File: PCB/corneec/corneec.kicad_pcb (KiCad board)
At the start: 2 copper layers, 226.8 x 157.6 mm, 80 parts, among them J1 OLED, J2 MJ-4PP-9, Q1 Q_NMOS_GSD, SW1 SW_Push, SW10 EC_SW, SW11 EC_SW, SW12 EC_SW, SW13 EC_SW, SW14 EC_SW, SW15 EC_SW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

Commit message: Update
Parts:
- removed the ? at (156.3, 68.6)
- removed the ? at (156.3, 49.9)
- removed the ? at (241.8, 47.4)
- removed the ? at (248.7, 95.2)
- removed the ? at (256.1, 112.6)
- removed the ? at (199.5, 85.9)
- removed the SW2 at (241.8, 56.9)
- removed the SW2 at (146.8, 59.2)
- removed the SW2 at (146.8, 40.2)
- removed the SW2 at (165.8, 40.2)
- removed the SW2 at (241.8, 75.9)
- removed the SW2 at (222.8, 35.5)
- removed the SW2 at (203.8, 71.1)
- removed the SW2 at (241.8, 37.9)
- removed the SW2 at (203.8, 52.1)
- removed the SW2 at (256.5, 99.6)
- removed the SW2 at (165.8, 59.2)
- removed the SW2 at (184.8, 35.5)
- removed the SW2 at (146.8, 78.2)
- removed the SW2 at (222.8, 73.5)
- removed the SW2 at (184.8, 54.5)
- removed the SW2 at (234.3, 95.9)
- removed the SW2 at (165.8, 78.2)
- removed the SW2 at (222.8, 54.5)
- removed the SW2 at (213.3, 93.2)
- removed the SW2 at (203.8, 33.1)
- removed the SW2 at (184.8, 73.5)
- moved ? 55.4 mm to (188.8, 97.3)
- moved C2 55.4 mm to (199.9, 104.3)
- moved H22 55.4 mm to (203.3, 105.8)
- moved J1 55.4 mm to (195.9, 89.5)
- moved J2 55.4 mm to (205.7, 98.6)
- moved JP2 55.4 mm to (186.0, 52.0)
- moved R2 55.4 mm to (158.9, 63.5)
- moved R3 55.4 mm to (181.1, 65.8)
- moved R4 55.4 mm to (120.9, 63.5)
- moved R5 55.4 mm to (101.9, 68.2)
- moved R7 55.4 mm to (82.9, 68.2)
- moved REF** 55.4 mm to (176.0, 65.8)
- moved REF** 55.4 mm to (90.5, 87.1)
- moved REF** 55.4 mm to (90.5, 68.3)
- moved SW10 55.4 mm to (119.0, 92.0)
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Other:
- board size 226.8 x 157.6 mm -> 133.8 x 91.4 mm

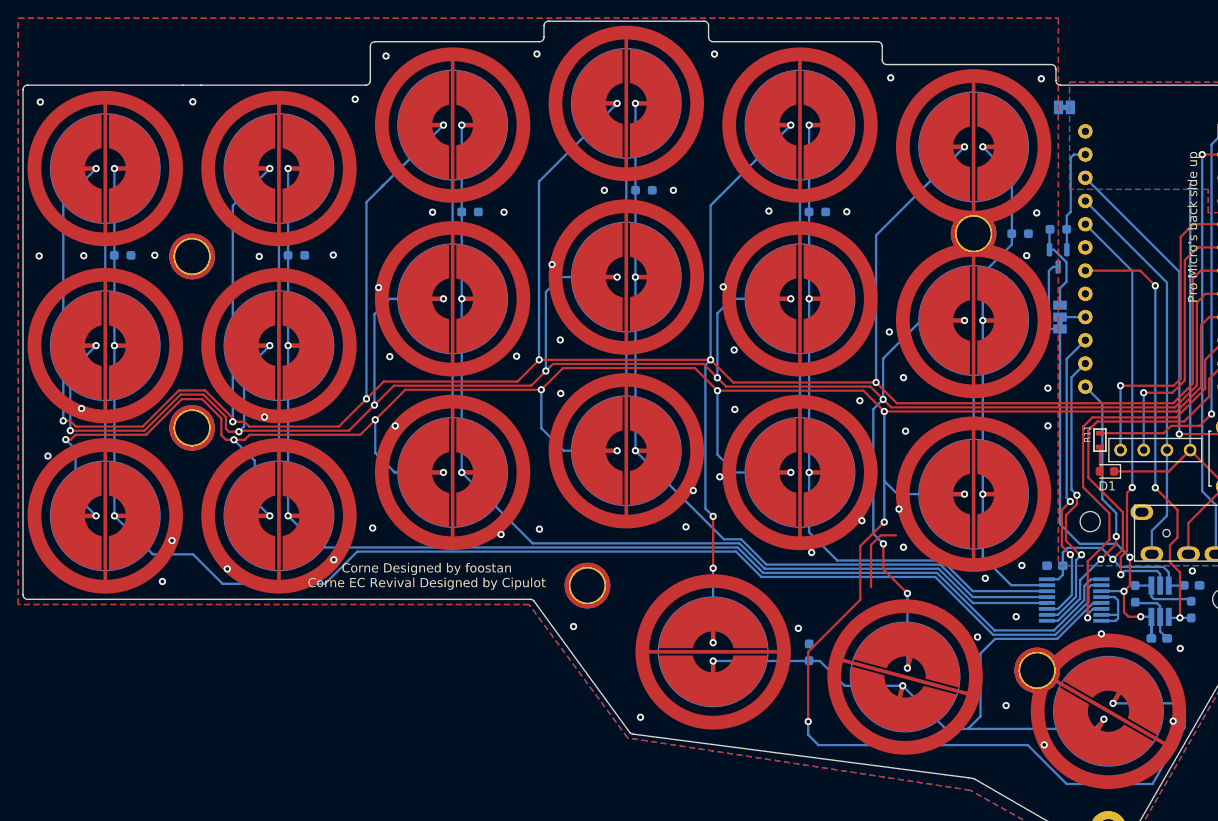
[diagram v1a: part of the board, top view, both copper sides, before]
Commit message: Updated EC pad footprint
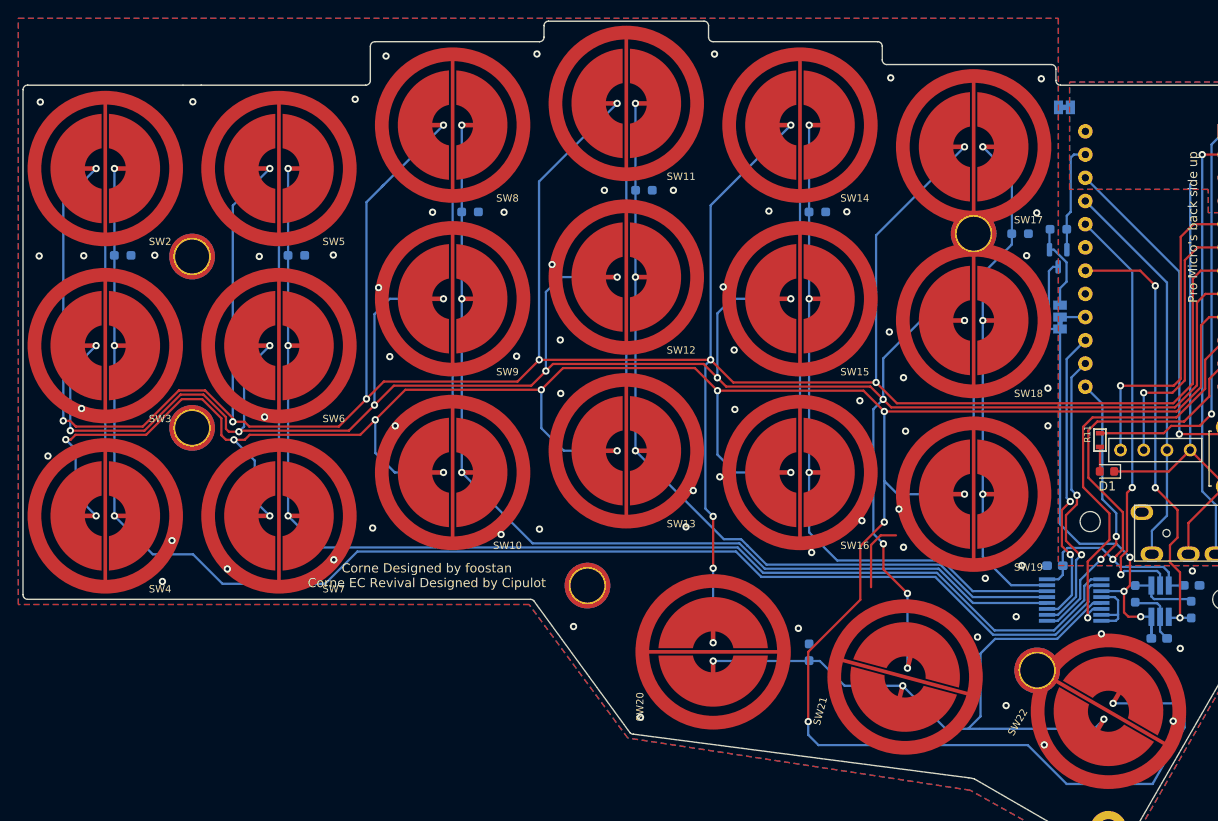
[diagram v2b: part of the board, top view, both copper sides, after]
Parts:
- R10: value 22k -> 22k : 100k
- U2: value LTC6255 -> LTC6255IS6TRMPBF_flipped_power
- renumbered SWe to SW7, SWe to SW9
